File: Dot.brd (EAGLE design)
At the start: 25.4 x 31.5 mm, 37 parts, among them IC1 CAT24M010TS, IC2 SI1145, U1 ATMEGA328P-MU-QFN32, U2 TMP102, U3 ISL29125, U4 9DoF IMU, U5 BMP18

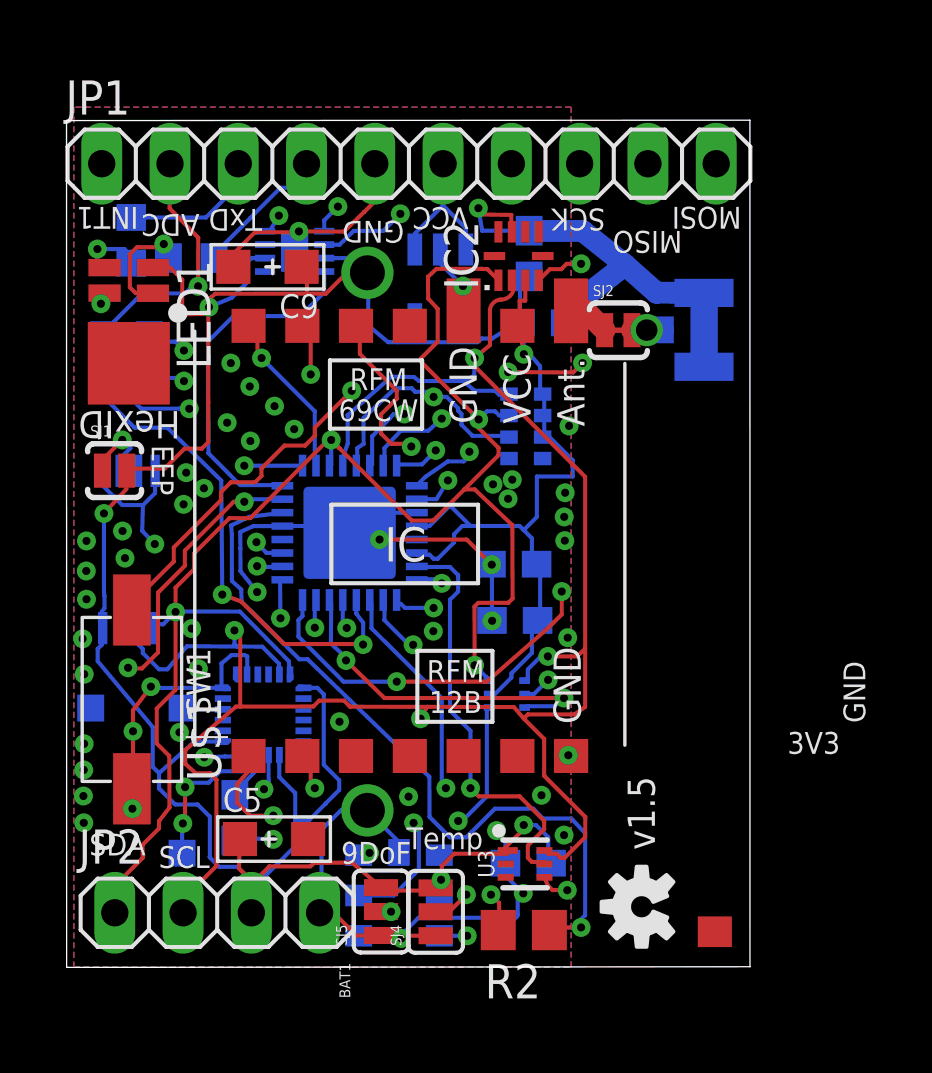
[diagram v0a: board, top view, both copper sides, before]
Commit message: Moving lower 100uF Cap to leave room fo the 3V3 and GND labels.
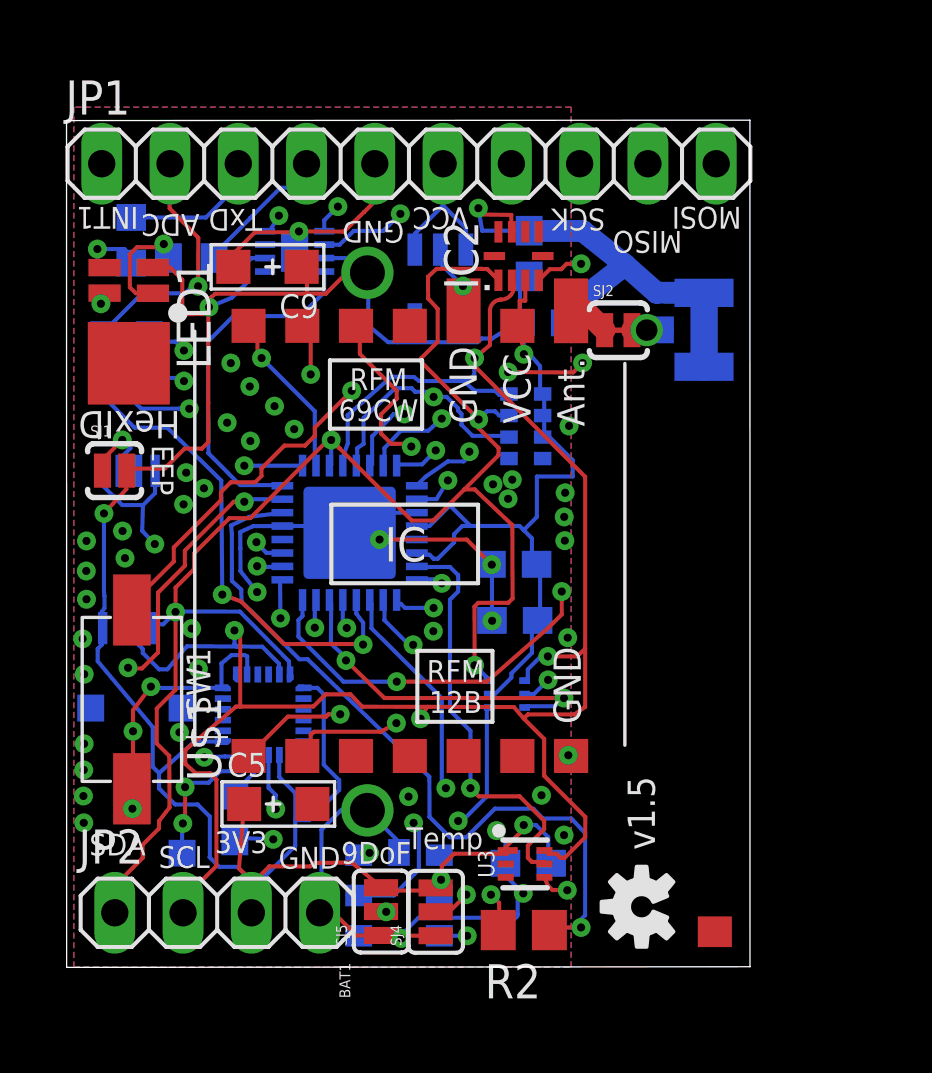
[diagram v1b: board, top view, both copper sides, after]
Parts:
- moved C5 1.31 mm to (8.23, 6.60)
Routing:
- net RSDO: track 16.3 -> 11.3 mm
- net +3V3: track 132.9 -> 134.3 mm
- net N$14: track 8.71 -> 8.13 mm
- net GND: vias 54 -> 53

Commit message: Added voltage divider for input voltage measuring.
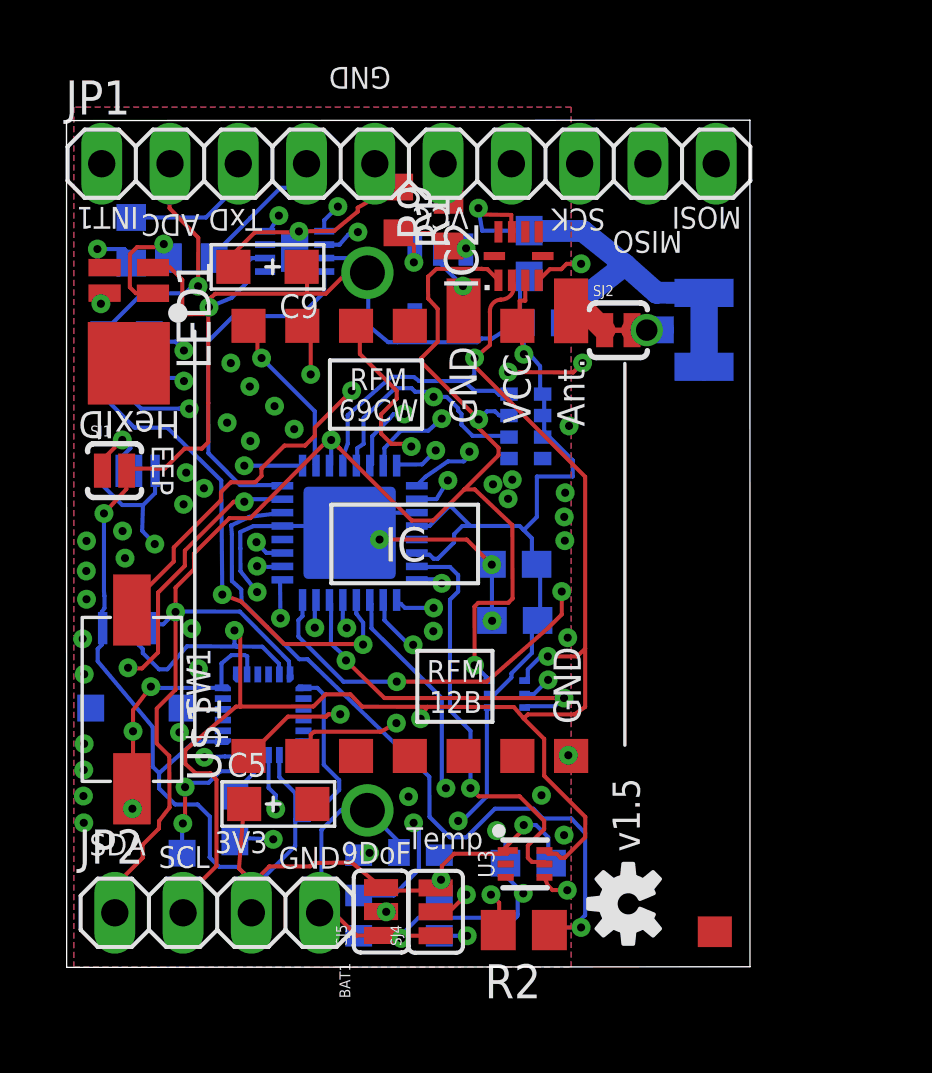
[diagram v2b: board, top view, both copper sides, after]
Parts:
- added R1, R9: (no value), resistor:R0603
- moved LOGO1 0.51 mm to (21.3, 2.88)
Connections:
- new net VIN_PIN: JP1.6, R9.2
- net GND: now also R1.1
- net VIN: now also R1.2, R9.1; no longer JP1.6
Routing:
- net VIN_PIN: track 0.00 -> 1.57 mm
- net SCK: track 41.4 -> 40.2 mm
- net VIN: track 5.62 -> 4.64 mm, vias 0 -> 2
- net GND: track 133.1 -> 134.1 mm

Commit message: Adding solderjumper for bypassing Voltage Regulator
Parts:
- added SJ3: SOLDERJUMPERNC2, SparkFun:SJ_2S-NOTRACE
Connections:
- net +3V3: now also SJ3.2
- net VIN: now also SJ3.1
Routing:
- net VIN: track 4.64 -> 5.38 mm
- net +3V3: track 134.3 -> 135.0 mm
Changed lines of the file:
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@@
 <layer number="21" name="tPlace" color="7" fill="1" visible="no" active="yes"/>
 <layer number="22" name="bPlace" color="7" fill="1" visible="no" active="yes"/>
-<layer number="23" name="tOrigins" color="15" fill="1" visible="no" active="yes"/>
-<layer number="24" name="bOrigins" color="15" fill="1" visible="no" active="yes"/>
+<layer number="23" name="tOrigins" color="15" fill="1" visible="yes" active="yes"/>
+<layer number="24" name="bOrigins" color="15" fill="1" visible="yes" active="yes"/>
 <layer number="25" name="tNames" color="7" fill="1" visible="no" active="yes"/>
 <layer number="26" name="bNames" color="7" fill="1" visible="no" active="yes"/>
@@
 <element name="R1" library="resistor" package="R0603" value="" x="12.700003125" y="28.695915625" rot="R270"/>
 <element name="R9" library="resistor" package="R0603" value="" x="14.56845" y="28.20383125" rot="R90"/>
+<element name="SJ3" library="SparkFun" package="SJ_2S-NOTRACE" value="SOLDERJUMPERNC2" x="13.3674125" y="25.69410625" rot="MR270"/>
 </elements>
 <signals>
@@
 <wire x1="6.945184375" y1="4.0273625" x2="6.945184375" y2="3.413978125" width="0.1524" layer="1"/>
 <wire x1="6.945184375" y1="3.413978125" x2="7.30605625" y2="3.05310625" width="0.1524" layer="1"/>
+<contactref element="SJ3" pad="2"/>
+<wire x1="13.3674125" y1="25.28140625" x2="13.313115625" y2="25.28140625" width="0.1524" layer="16"/>
+<wire x1="13.313115625" y1="25.28140625" x2="13.313115625" y2="24.62186875" width="0.1524" layer="16"/>
 </signal>
 <signal name="ADCENA">
@@
 <wire x1="15.21884375" y1="27.266821875" x2="15.1899125" y2="27.245271875" width="0.1524" layer="16"/>
 <wire x1="15.1899125" y1="27.245271875" x2="15.213115625" y2="27.22206875" width="0.1524" layer="16"/>
+<contactref element="SJ3" pad="1"/>
+<wire x1="13.3674125" y1="26.09500625" x2="13.27670625" y2="26.09500625" width="0.1524" layer="16"/>
+<wire x1="13.27670625" y1="26.09500625" x2="13.27670625" y2="26.746021875" width="0.1524" layer="16"/>
 </signal>
 <signal name="N$1">

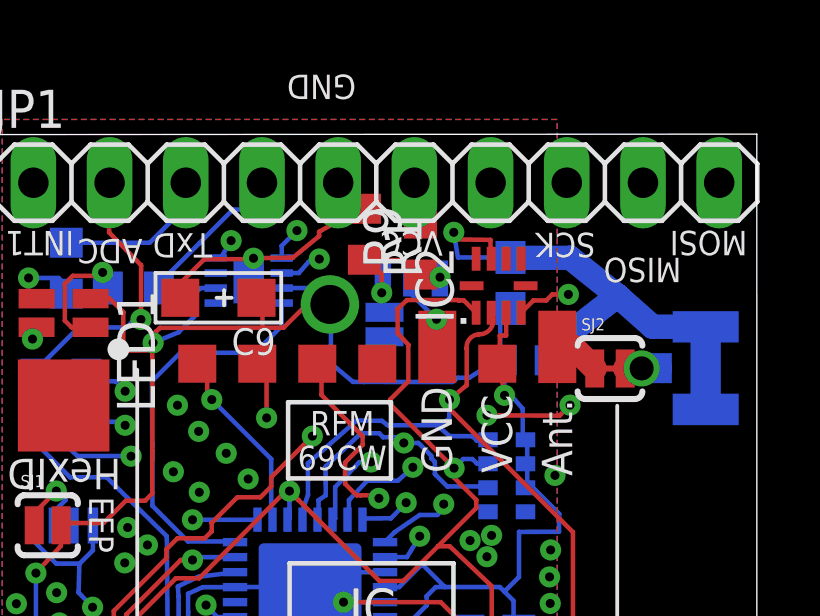
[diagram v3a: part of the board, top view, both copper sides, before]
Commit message: Added cap for Reset via DTR pin / Easy Arduino upload
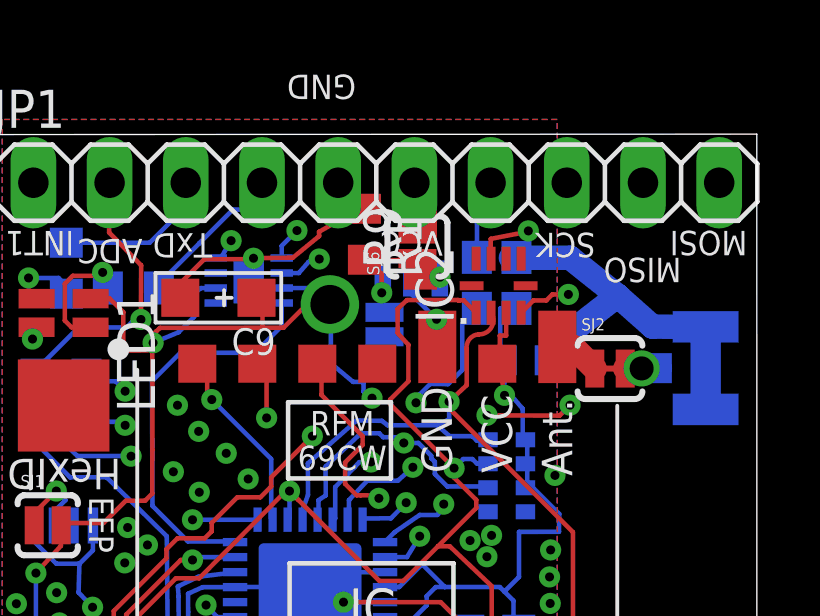
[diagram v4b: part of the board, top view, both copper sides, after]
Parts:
- added C7: 0.1uF, resistor:C0603
- added SJ6: SOLDERJUMPERNC2, SparkFun:SJ_2S-NOTRACE
- moved C6 0.20 mm to (17.8, 27.1)
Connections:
- new net N$5: C7.2, JP1.7
- net RST: now also C7.1; no longer JP1.7
- net VIN: now also SJ6.1
- net VIN_PIN: now also SJ6.2
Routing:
- net RST: track 19.3 -> 14.7 mm, vias 1 -> 2
- net N$5: track 0.00 -> 2.68 mm
- net +3V3: track 135.0 -> 136.9 mm, vias 7 -> 8
